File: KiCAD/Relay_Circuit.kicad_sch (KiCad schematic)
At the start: 6 parts, among them K1 G5V-1, U1 PC365NJ0000F

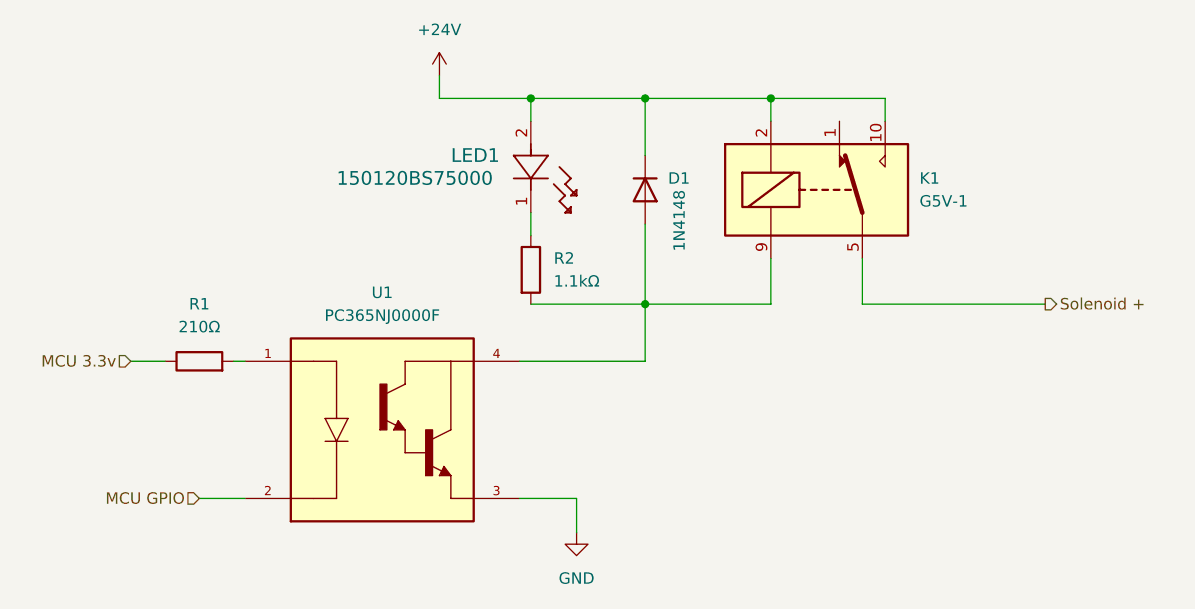
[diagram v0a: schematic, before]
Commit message: Ran Annotation and ERC
Annotated and ran Electronics Rules Checker. Started assigning footprints and appropriate step files to said footprints. Added custom KiCAD library folder to Github.
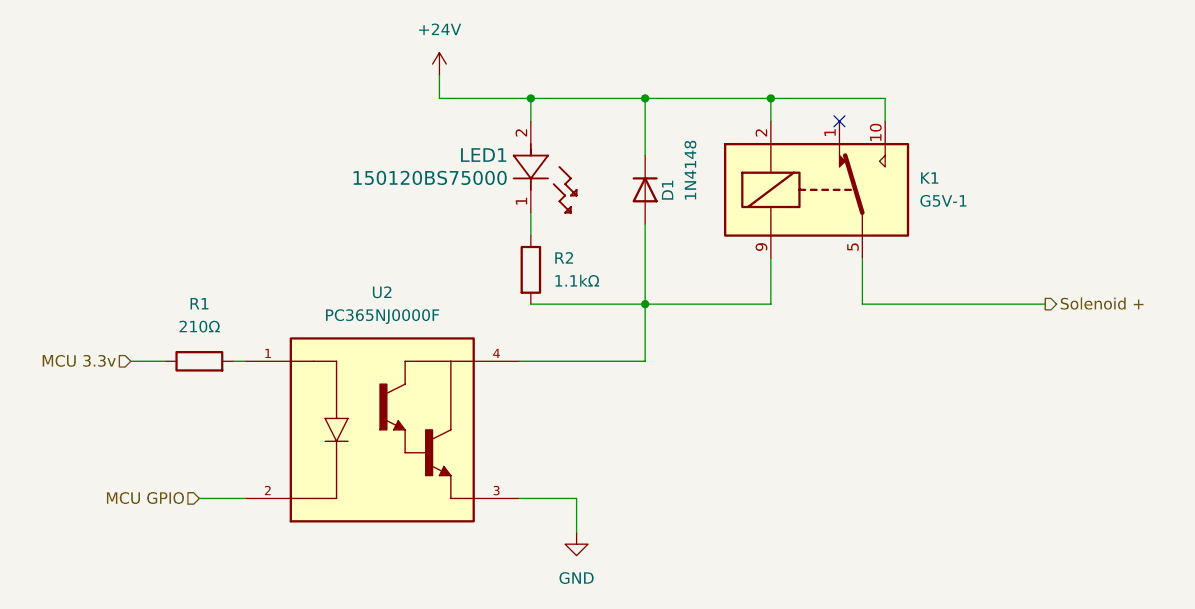
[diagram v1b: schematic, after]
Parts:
- LED1: footprint LED_150120RS75000_WRE -> LED_150120BS75000:LED_150120RS75000_WRE
- renumbered U1 to U2
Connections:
- no-connect marks 0 -> 1

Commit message: Started PCB layout
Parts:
- R1, R2: footprint (none) -> Resistor_THT:R_Axial_DIN0204_L3.6mm_D1.6mm_P5.08mm_Horizontal
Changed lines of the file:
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@@
       (effects (font (size 1.27 1.27)) (justify left))
     )
-    (property "Footprint" "" (at 160.782 82.55 90)
+    (property "Footprint" "Resistor_THT:R_Axial_DIN0204_L3.6mm_D1.6mm_P5.08mm_Horizontal" (at 160.782 82.55 90)
       (effects (font (size 1.27 1.27)) hide)
     )
@@
       (effects (font (size 1.27 1.27)))
     )
-    (property "Footprint" "" (at 125.73 94.488 90)
+    (property "Footprint" "Resistor_THT:R_Axial_DIN0204_L3.6mm_D1.6mm_P5.08mm_Horizontal" (at 125.73 94.488 90)
       (effects (font (size 1.27 1.27)) hide)
     )

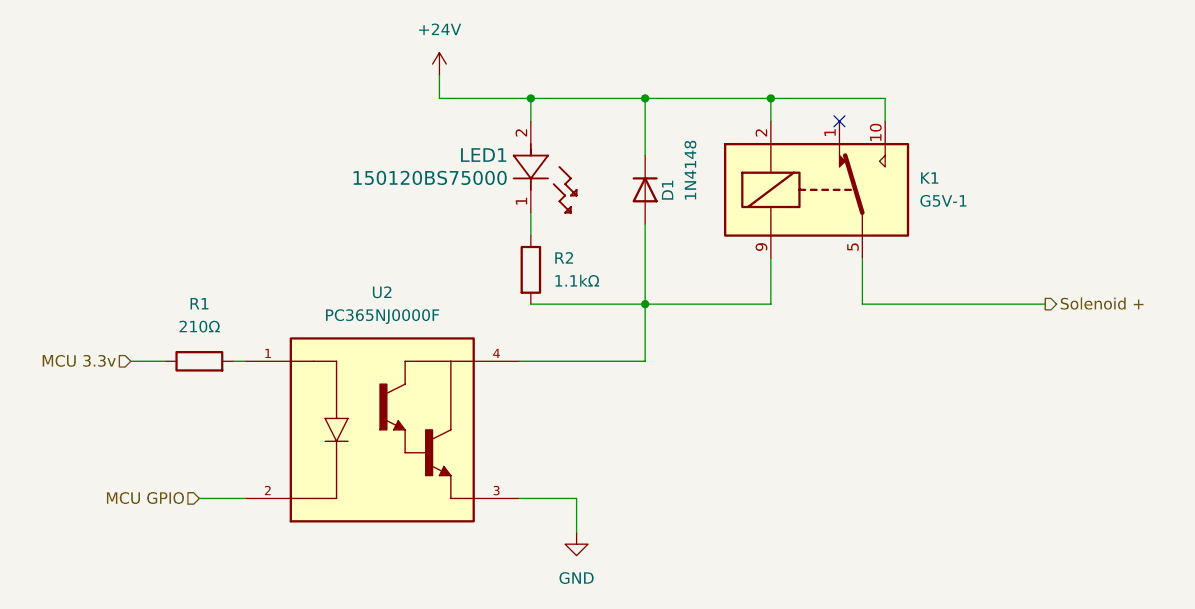
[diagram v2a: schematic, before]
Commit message: Changed to tht LEDs and added LED to power monitor circuit
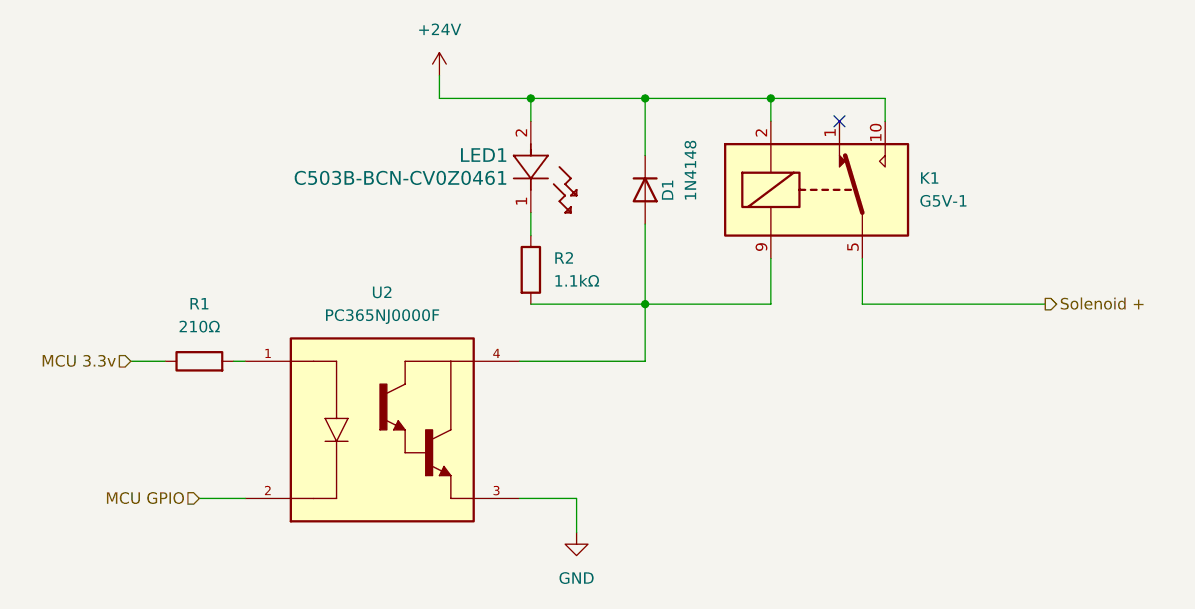
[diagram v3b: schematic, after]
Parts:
- removed LED1: 150120BS75000, LED_150120BS75000:LED_150120RS75000_WRE, symbol LED_150120BS75000:150120BS75000
- added LED1: C503B-BCN-CV0Z0461, CreeLED Blue:C503B_BCN_CV0Z0461, symbol CreeLED Blue:C503B-BCN-CV0Z0461
- U2: footprint PC365NJ0000F:SOIC254P700X280-4N -> PC365NJ0000F:PC365NJ0000F
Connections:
- net +24V: now also LED1.2
- net at R2.1: now also LED1.1
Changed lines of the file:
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@@
     )
   )
-  (symbol (lib_id "PC365NJ0000F:PC365NJ0000F") (at 146.05 100.33 0) (unit 1)
-    (in_bom yes) (on_board yes) (dnp no) (fields_autoplaced)
-    (property "Reference" "U2" (at 146.05 85.09 0)
-      (effects (font (size 1.27 1.27)))
+  (symbol (lib_id "CreeLED Blue:C503B-BCN-CV0Z0461") (at 162.56 66.04 270) (unit 1)
+    (in_bom yes) (on_board yes) (dnp no)
+    (property "Reference" "LED1" (at 160.02 69.85 90)
+      (effects (font (size 1.524 1.524)) (justify right))
     )
-    (property "Value" "PC365NJ0000F" (at 146.05 87.63 0)
-      (effects (font (size 1.27 1.27)))
+    (property "Value" "C503B-BCN-CV0Z0461" (at 160.02 72.39 90)
+      (effects (font (size 1.524 1.524)) (justify right))
     )
-    (property "Footprint" "PC365NJ0000F:SOIC254P700X280-4N" (at 146.05 100.33 0)
-      (effects (font (size 1.27 1.27)) (justify bottom) hide)
+    (property "Footprint" "CreeLED Blue:C503B_BCN_CV0Z0461" (at 162.56 66.04 0)
+      (effects (font (size 1.27 1.27) italic) hide)
     )
-    (property "Datasheet" "" (at 146.05 100.33 0)
-      (effects (font (size 1.27 1.27)) hide)
+    (property "Datasheet" "C503B-BCN-CV0Z0461" (at 162.56 66.04 0)
+      (effects (font (size 1.27 1.27) italic) hide)
     )
-    (property "PARTREV" "Jun. 30. 2005" (at 146.05 100.33 0)
-      (effects (font (size 1.27 1.27)) (justify bottom) hide)
-    )
-    (property "MANUFACTURER" "Sharp" (at 146.05 100.33 0)
-      (effects (font (size 1.27 1.27)) (justify bottom) hide)
-    )
-    (property "MAXIMUM_PACKAGE_HEIGHT" "2.80mm" (at 146.05 100.33 0)
-      (effects (font (size 1.27 1.27)) (justify bottom) hide)
-    )
-    (property "STANDARD" "IPC-7351B" (at 146.05 100.33 0)
-      (effects (font (size 1.27 1.27)) (justify bottom) hide)
-    )
+    (pin "2")
     (pin "1")
-    (pin "4")
-    (pin "3")
-    (pin "2")
     (instances
       (project "ColletAutoFeed_RelayBoard"
         (path "/603d0a2e-fca7-40af-8fa8-51b59d823d4d/f85cc271-3b11-4af6-88e7-0089384d0a70"
-          (reference "U2") (unit 1)
+          (reference "LED1") (unit 1)
         )
         (path "/603d0a2e-fca7-40af-8fa8-51b59d823d4d/1b4c4683-ae7a-43db-9c55-2e017b2b64f6"
-          (reference "U3") (unit 1)
+          (reference "LED2") (unit 1)
+        )
+        (path "/603d0a2e-fca7-40af-8fa8-51b59d823d4d/c99ad83c-1e55-4897-95dc-696fc040ab27"
+          (reference "LED3") (unit 1)
         )
         (path "/603d0a2e-fca7-40af-8fa8-51b59d823d4d/bf76bbb3-62c3-43bd-a097-b9f452e57b35"
-          (reference "U5") (unit 1)
+          (reference "LED4") (unit 1)
+        )
+        (path "/603d0a2e-fca7-40af-8fa8-51b59d823d4d/c4c73976-bc86-4ae3-8f28-ea5e6a098449"
+          (reference "LED5") (unit 1)
         )
         (path "/603d0a2e-fca7-40af-8fa8-51b59d823d4d/1e7f4279-2019-4687-9b9a-14c5bef026a1"
-          (reference "U7") (unit 1)
+          (reference "LED6") (unit 1)
+        )
+        (path "/603d0a2e-fca7-40af-8fa8-51b59d823d4d/e9594ab2-eb4a-412d-b212-c8b9b51a6168"
+          (reference "LED7") (unit 1)
         )
         (path "/603d0a2e-fca7-40af-8fa8-51b59d823d4d/b14b409f-5174-4f0c-b56e-0f620ad960f8"
-          (reference "U9") (unit 1)
-        )
-        (path "/603d0a2e-fca7-40af-8fa8-51b59d823d4d/c99ad83c-1e55-4897-95dc-696fc040ab27"
-          (reference "U4") (unit 1)
-        )
-        (path "/603d0a2e-fca7-40af-8fa8-51b59d823d4d/c4c73976-bc86-4ae3-8f28-ea5e6a098449"
-          (reference "U6") (unit 1)
-        )
-        (path "/603d0a2e-fca7-40af-8fa8-51b59d823d4d/e9594ab2-eb4a-412d-b212-c8b9b51a6168"
-          (reference "U8") (unit 1)
+          (reference "LED8") (unit 1)
         )
       )
@@
     )
   )
-  (symbol (lib_id "LED_150120BS75000:150120BS75000") (at 162.56 66.04 270) (unit 1)
-    (in_bom yes) (on_board yes) (dnp no)
-    (property "Reference" "LED1" (at 160.02 69.85 90)
-      (effects (font (size 1.524 1.524)) (justify right))
+  (symbol (lib_id "PC365NJ0000F:PC365NJ0000F") (at 146.05 100.33 0) (unit 1)
+    (in_bom yes) (on_board yes) (dnp no) (fields_autoplaced)
+    (property "Reference" "U2" (at 146.05 85.09 0)
+      (effects (font (size 1.27 1.27)))
     )
-    (property "Value" "150120BS75000" (at 160.02 72.39 90)
-      (effects (font (size 1.524 1.524)) (justify right))
+    (property "Value" "PC365NJ0000F" (at 146.05 87.63 0)
+      (effects (font (size 1.27 1.27)))
     )
-    (property "Footprint" "LED_150120BS75000:LED_150120RS75000_WRE" (at 172.72 66.04 0)
-      (effects (font (size 1.27 1.27) italic) hide)
+    (property "Footprint" "PC365NJ0000F:PC365NJ0000F" (at 146.05 100.33 0)
+      (effects (font (size 1.27 1.27)) (justify bottom) hide)
     )
-    (property "Datasheet" "150120BS75000" (at 170.18 66.04 0)
-      (effects (font (size 1.27 1.27) italic) hide)
+    (property "Datasheet" "" (at 146.05 100.33 0)
+      (effects (font (size 1.27 1.27)) hide)
+    )
+    (property "PARTREV" "Jun. 30. 2005" (at 146.05 100.33 0)
+      (effects (font (size 1.27 1.27)) (justify bottom) hide)
+    )
+    (property "MANUFACTURER" "Sharp" (at 146.05 100.33 0)
+      (effects (font (size 1.27 1.27)) (justify bottom) hide)
+    )
+    (property "MAXIMUM_PACKAGE_HEIGHT" "2.80mm" (at 146.05 100.33 0)
+      (effects (font (size 1.27 1.27)) (justify bottom) hide)
+    )
+    (property "STANDARD" "IPC-7351B" (at 146.05 100.33 0)
+      (effects (font (size 1.27 1.27)) (justify bottom) hide)
     )
     (pin "1")
     (pin "2")
+    (pin "3")
+    (pin "4")
     (instances
       (project "ColletAutoFeed_RelayBoard"
         (path "/603d0a2e-fca7-40af-8fa8-51b59d823d4d/f85cc271-3b11-4af6-88e7-0089384d0a70"
-          (reference "LED1") (unit 1)
+          (reference "U2") (unit 1)
         )
         (path "/603d0a2e-fca7-40af-8fa8-51b59d823d4d/1b4c4683-ae7a-43db-9c55-2e017b2b64f6"
-          (reference "LED2") (unit 1)
+          (reference "U3") (unit 1)
         )
         (path "/603d0a2e-fca7-40af-8fa8-51b59d823d4d/c99ad83c-1e55-4897-95dc-696fc040ab27"
-          (reference "LED3") (unit 1)
+          (reference "U4") (unit 1)
         )
         (path "/603d0a2e-fca7-40af-8fa8-51b59d823d4d/bf76bbb3-62c3-43bd-a097-b9f452e57b35"
-          (reference "LED4") (unit 1)
+          (reference "U5") (unit 1)
         )
         (path "/603d0a2e-fca7-40af-8fa8-51b59d823d4d/c4c73976-bc86-4ae3-8f28-ea5e6a098449"
-          (reference "LED5") (unit 1)
+          (reference "U6") (unit 1)
         )
         (path "/603d0a2e-fca7-40af-8fa8-51b59d823d4d/1e7f4279-2019-4687-9b9a-14c5bef026a1"
-          (reference "LED6") (unit 1)
+          (reference "U7") (unit 1)
         )
         (path "/603d0a2e-fca7-40af-8fa8-51b59d823d4d/e9594ab2-eb4a-412d-b212-c8b9b51a6168"
-          (reference "LED7") (unit 1)
+          (reference "U8") (unit 1)
         )
         (path "/603d0a2e-fca7-40af-8fa8-51b59d823d4d/b14b409f-5174-4f0c-b56e-0f620ad960f8"
-          (reference "LED8") (unit 1)
+          (reference "U9") (unit 1)
         )
       )

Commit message: Started routing
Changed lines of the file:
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@@
+    (stroke (width 0) (type default))
+  )
+  (wire (pts (xy 130.81 92.71) (xy 129.54 92.71))
     (stroke (width 0) (type default))
   )
@@
   )
   (wire (pts (xy 162.56 86.36) (xy 175.26 86.36))
-    (stroke (width 0) (type default))
-  )
-  (wire (pts (xy 129.54 92.71) (xy 130.81 92.71))
     (stroke (width 0) (type default))
   )
@@
     (effects (font (size 1.27 1.27)) (justify left))
   )
+  (netclass_flag "" (length 1) (shape round) (at 129.54 92.71 0) (fields_autoplaced)
+    (effects (font (size 1.27 1.27)) (justify left bottom))
+    (property "Netclass" "signal" (at 130.2385 91.71 0)
+      (effects (font (size 1.27 1.27) italic) (justify left) hide)
+    )
+  )
+  (netclass_flag "" (length 1) (shape round) (at 165.1 92.71 180) (fields_autoplaced)
+    (effects (font (size 1.27 1.27)) (justify right bottom))
+    (property "Netclass" "power" (at 165.7985 93.71 0)
+      (effects (font (size 1.27 1.27) italic) (justify left) hide)
+    )
+  )
+  (netclass_flag "" (length 1) (shape round) (at 162.56 77.47 90) (fields_autoplaced)
+    (effects (font (size 1.27 1.27)) (justify left bottom))
+    (property "Netclass" "power" (at 161.56 76.7715 90)
+      (effects (font (size 1.27 1.27) italic) (justify left) hide)
+    )
+  )
   (symbol (lib_id "Relay:G5V-1") (at 194.31 73.66 0) (unit 1)

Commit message: Continued working on routing
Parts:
- R1: footprint Resistor_THT:R_Axial_DIN0204_L3.6mm_D1.6mm_P5.08mm_Horizontal -> Resistor:R_Axial_DIN0204_L3.6mm_D1.6mm_P5.08mm_Horizontal-JW
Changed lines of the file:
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@@
       (effects (font (size 1.27 1.27)))
     )
-    (property "Footprint" "Resistor_THT:R_Axial_DIN0204_L3.6mm_D1.6mm_P5.08mm_Horizontal" (at 125.73 94.488 90)
+    (property "Footprint" "Resistor:R_Axial_DIN0204_L3.6mm_D1.6mm_P5.08mm_Horizontal-JW" (at 125.73 94.488 90)
       (effects (font (size 1.27 1.27)) hide)
     )

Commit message: Updated resistor footprints to include values
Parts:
- R2: footprint Resistor_THT:R_Axial_DIN0204_L3.6mm_D1.6mm_P5.08mm_Horizontal -> Resistor:R_Axial_DIN0204_L3.6mm_D1.6mm_P5.08mm_Horizontal-JW
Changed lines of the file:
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@@
       (effects (font (size 1.27 1.27)) (justify left))
     )
-    (property "Footprint" "Resistor_THT:R_Axial_DIN0204_L3.6mm_D1.6mm_P5.08mm_Horizontal" (at 160.782 82.55 90)
+    (property "Footprint" "Resistor:R_Axial_DIN0204_L3.6mm_D1.6mm_P5.08mm_Horizontal-JW" (at 160.782 82.55 90)
       (effects (font (size 1.27 1.27)) hide)
     )
